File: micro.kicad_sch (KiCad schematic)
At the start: 18 parts, among them J15 Conn_01x02, J16 Conn_01x03, J17 Conn_01x08, J18 Conn_01x02, J19 Conn_01x02, SW2 SW_MEC_5G_LED

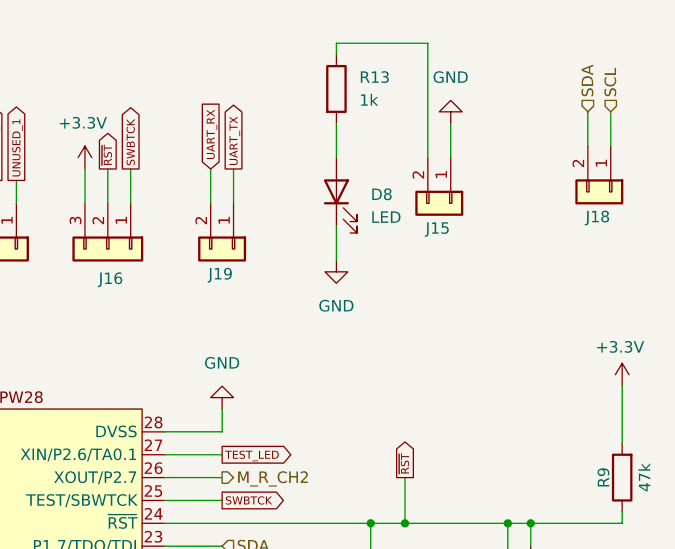
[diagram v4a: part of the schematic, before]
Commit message: minor update to an MCU circuit
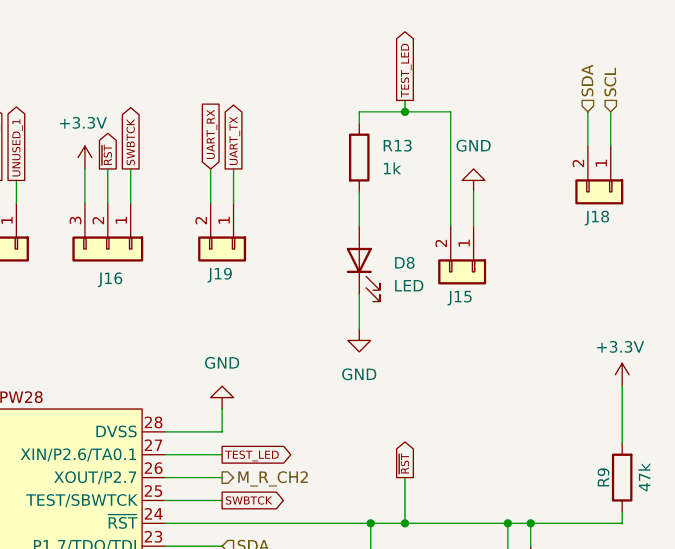
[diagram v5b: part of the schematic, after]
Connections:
- net TEST_LED: now also J15.2 (Pin_2), R13.1
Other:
- moved on the sheet: D8, J15, R13
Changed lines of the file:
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@@
 	)
 	(junction
+		(at 163.83 22.86)
+		(diameter 0)
+		(color 0 0 0 0)
+	)
+	(junction
 		(at 163.83 68.58)
 		(diameter 0)
@@
 	(wire
 		(pts
-			(xy 168.91 24.13) (xy 168.91 27.94)
+			(xy 171.45 31.75) (xy 171.45 35.56)
 		)
 		(stroke
@@
 	(wire
 		(pts
-			(xy 156.21 24.13) (xy 156.21 27.94)
+			(xy 158.75 31.75) (xy 158.75 35.56)
 		)
 		(stroke
@@
 	(wire
 		(pts
+			(xy 163.83 22.86) (xy 158.75 22.86)
+		)
+		(stroke
+			(width 0)
+			(type default)
+		)
+	)
+	(wire
+		(pts
 			(xy 163.83 63.5) (xy 163.83 68.58)
 		)
@@
 	(wire
 		(pts
-			(xy 156.21 35.56) (xy 156.21 39.37)
+			(xy 158.75 43.18) (xy 158.75 46.99)
 		)
 		(stroke
@@
 	(wire
 		(pts
-			(xy 166.37 15.24) (xy 156.21 15.24)
+			(xy 168.91 22.86) (xy 163.83 22.86)
 		)
 		(stroke
@@
 	(wire
 		(pts
+			(xy 163.83 21.59) (xy 163.83 22.86)
+		)
+		(stroke
+			(width 0)
+			(type default)
+		)
+	)
+	(wire
+		(pts
 			(xy 86.36 76.2) (xy 90.17 76.2)
 		)
@@
 	(wire
 		(pts
-			(xy 156.21 15.24) (xy 156.21 16.51)
+			(xy 158.75 22.86) (xy 158.75 24.13)
 		)
 		(stroke
@@
 	(wire
 		(pts
-			(xy 166.37 27.94) (xy 166.37 15.24)
+			(xy 168.91 35.56) (xy 168.91 22.86)
 		)
 		(stroke
@@
 		)
 	)
+	(global_label "TEST_LED"
+		(shape output)
+		(at 163.83 21.59 90)
+		(fields_autoplaced yes)
+		(effects
+			(font
+				(size 0.889 0.889)
+			)
+			(justify left)
+		)
+		(property "Intersheetrefs" "${INTERSHEET_REFS}"
+			(at 163.83 13.4046 90)
+			(effects
+				(font
+					(size 1.27 1.27)
+				)
+				(justify left)
+				(hide yes)
+			)
+		)
+	)
 	(global_label "UNUSED_3"
 		(shape output)
@@
 	(symbol
 		(lib_id "Device:LED")
-		(at 156.21 31.75 90)
+		(at 158.75 39.37 90)
 		(unit 1)
 		(exclude_from_sim no)
@@
 		(fields_autoplaced yes)
 		(property "Reference" "D8"
-			(at 160.02 32.0674 90)
+			(at 162.56 39.6874 90)
 			(effects
 				(font
@@
 		)
 		(property "Value" "LED"
-			(at 160.02 34.6074 90)
+			(at 162.56 42.2274 90)
 			(effects
 				(font
@@
 		)
 		(property "Footprint" "LED_SMD:LED_1210_3225Metric"
-			(at 156.21 31.75 0)
+			(at 158.75 39.37 0)
 			(effects
 				(font
@@
 		)
 		(property "Datasheet" "~"
-			(at 156.21 31.75 0)
+			(at 158.75 39.37 0)
 			(effects
 				(font
@@
 		)
 		(property "Description" "Light emitting diode"
-			(at 156.21 31.75 0)
+			(at 158.75 39.37 0)
 			(effects
 				(font
@@
 		)
 		(property "Sim.Pins" "1=K 2=A"
-			(at 156.21 31.75 0)
+			(at 158.75 39.37 0)
 			(effects
 				(font
@@
 	(symbol
 		(lib_id "power:GND")
-		(at 168.91 24.13 180)
+		(at 171.45 31.75 180)
 		(unit 1)
 		(exclude_from_sim no)
@@
 		(fields_autoplaced yes)
 		(property "Reference" "#PWR055"
-			(at 168.91 17.78 0)
+			(at 171.45 25.4 0)
 			(effects
 				(font
@@
 		)
 		(property "Value" "GND"
-			(at 168.91 19.05 0)
+			(at 171.45 26.67 0)
 			(effects
 				(font
@@
 		)
 		(property "Footprint" ""
-			(at 168.91 24.13 0)
+			(at 171.45 31.75 0)
 			(effects
 				(font
@@
 		)
 		(property "Datasheet" ""
-			(at 168.91 24.13 0)
+			(at 171.45 31.75 0)
 			(effects
 				(font
@@
 		)
 		(property "Description" "Power symbol creates a global label with name \"GND\" , ground"
-			(at 168.91 24.13 0)
+			(at 171.45 31.75 0)
 			(effects
 				(font
@@
 	(symbol
 		(lib_id "Connector_Generic:Conn_01x02")
-		(at 168.91 33.02 270)
+		(at 171.45 40.64 270)
 		(unit 1)
 		(exclude_from_sim no)
@@
 		(dnp no)
 		(property "Reference" "J15"
-			(at 166.116 35.814 90)
+			(at 168.656 43.434 90)
 			(effects
 				(font
@@
 		)
 		(property "Value" "Conn_01x02"
-			(at 171.45 34.2899 90)
+			(at 173.99 41.9099 90)
 			(effects
 				(font
@@
 		)
 		(property "Footprint" ""
-			(at 168.91 33.02 0)
+			(at 171.45 40.64 0)
 			(effects
 				(font
@@
 		)
 		(property "Datasheet" "~"
-			(at 168.91 33.02 0)
+			(at 171.45 40.64 0)
 			(effects
 				(font
@@
 		)
 		(property "Description" "Generic connector, single row, 01x02, script generated (kicad-library-utils/schlib/autogen/connector/)"
-			(at 168.91 33.02 0)
+			(at 171.45 40.64 0)
 			(effects
 				(font
@@
 	(symbol
 		(lib_id "power:GND")
-		(at 156.21 39.37 0)
+		(at 158.75 46.99 0)
 		(unit 1)
 		(exclude_from_sim no)
@@
 		(fields_autoplaced yes)
 		(property "Reference" "#PWR056"
-			(at 156.21 45.72 0)
+			(at 158.75 53.34 0)
 			(effects
 				(font
@@
 		)
 		(property "Value" "GND"
-			(at 156.21 44.45 0)
+			(at 158.75 52.07 0)
 			(effects
 				(font
@@
 		)
 		(property "Footprint" ""
-			(at 156.21 39.37 0)
+			(at 158.75 46.99 0)
 			(effects
 				(font
@@
 		)
 		(property "Datasheet" ""
-			(at 156.21 39.37 0)
+			(at 158.75 46.99 0)
 			(effects
 				(font
@@
 		)
 		(property "Description" "Power symbol creates a global label with name \"GND\" , ground"
-			(at 156.21 39.37 0)
+			(at 158.75 46.99 0)
 			(effects
 				(font
@@
 	(symbol
 		(lib_id "Device:R")
-		(at 156.21 20.32 0)
+		(at 158.75 27.94 0)
 		(unit 1)
 		(exclude_from_sim no)
@@
 		(fields_autoplaced yes)
 		(property "Reference" "R13"
-			(at 158.75 19.0499 0)
+			(at 161.29 26.6699 0)
 			(effects
 				(font
@@
 		)
 		(property "Value" "1k"
-			(at 158.75 21.5899 0)
+			(at 161.29 29.2099 0)
 			(effects
 				(font
@@
 		)
 		(property "Footprint" "Resistor_SMD:R_1210_3225Metric"
-			(at 154.432 20.32 90)
+			(at 156.972 27.94 90)
 			(effects
 				(font
@@
 		)
 		(property "Datasheet" "~"
-			(at 156.21 20.32 0)
+			(at 158.75 27.94 0)
 			(effects
 				(font
@@
 		)
 		(property "Description" "Resistor"
-			(at 156.21 20.32 0)
+			(at 158.75 27.94 0)
 			(effects
 				(font
